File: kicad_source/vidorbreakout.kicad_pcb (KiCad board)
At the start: 2 copper layers, 40 x 46.5 mm, 12 parts, among them CN1 TE_2041119-2, CN2 CONN_01X18, CN3 CONN_01X18

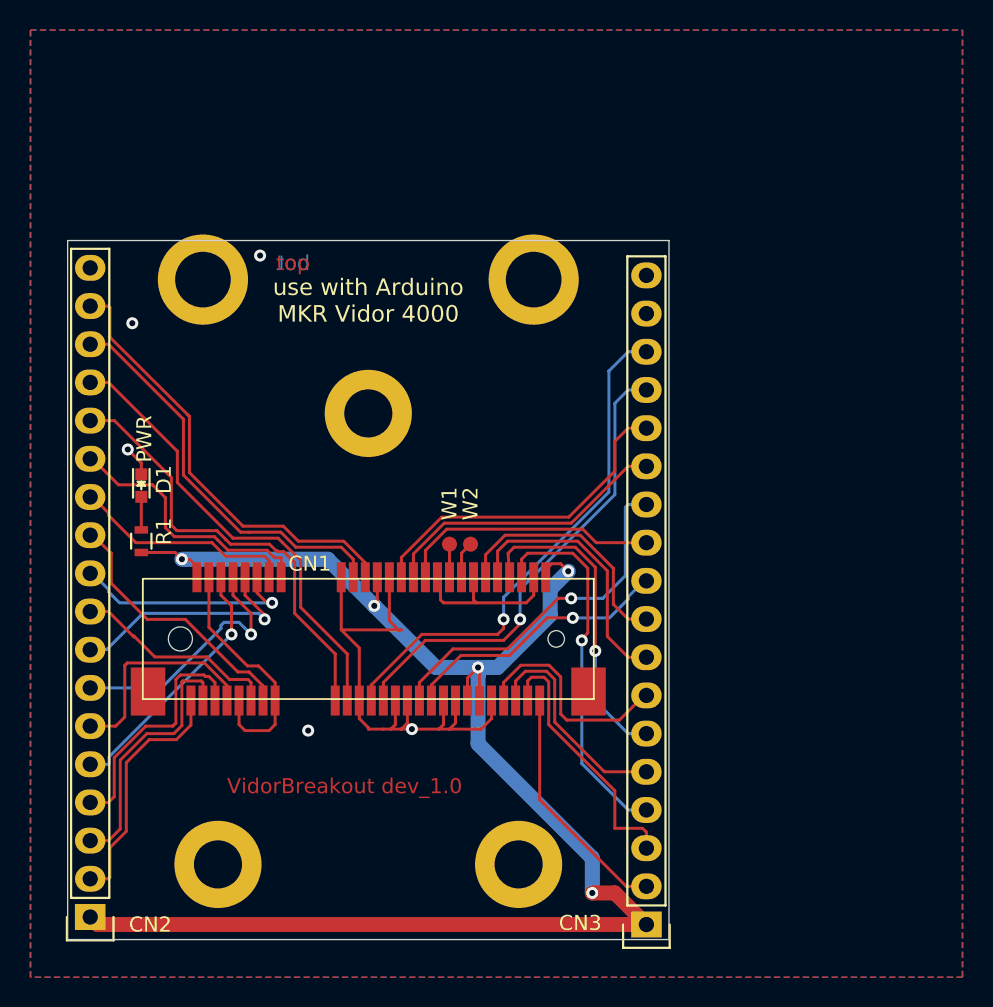
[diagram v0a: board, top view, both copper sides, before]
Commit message: aligned pin header to grid
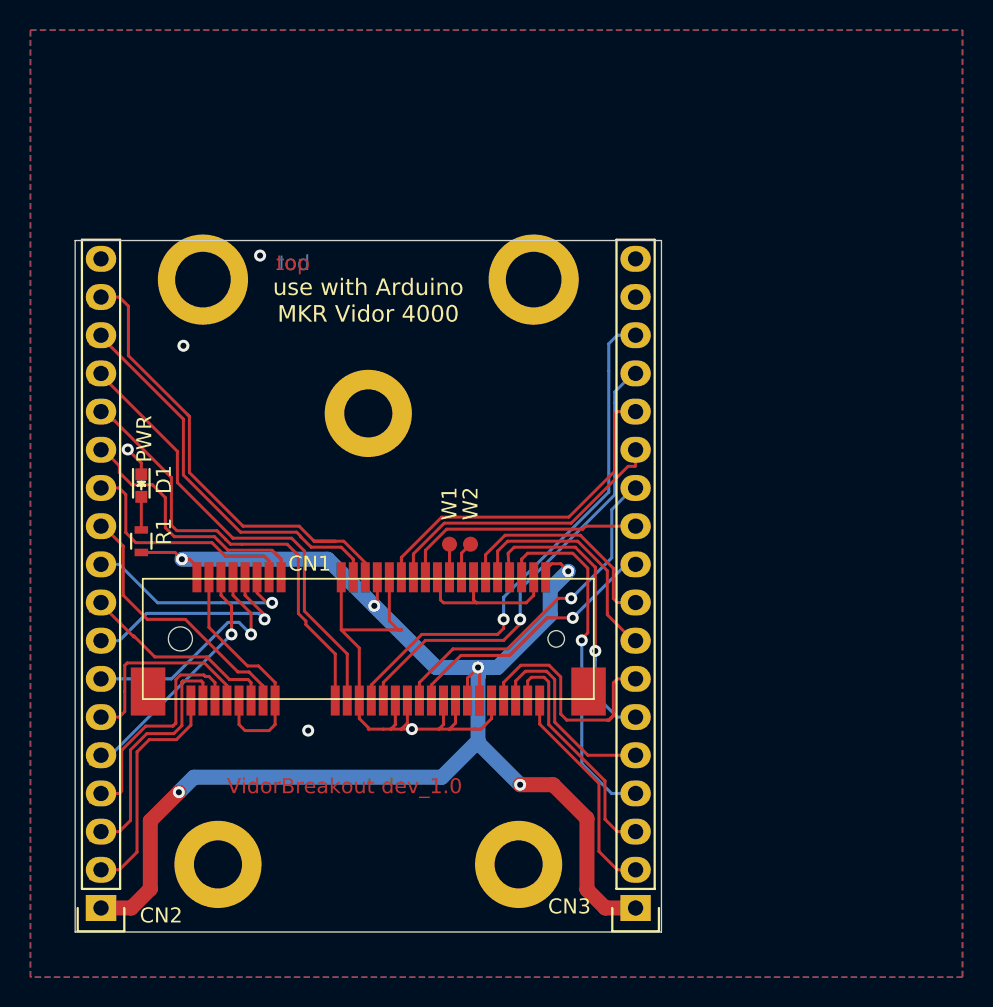
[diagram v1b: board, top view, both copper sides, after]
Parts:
- moved CN3 1.31 mm to (112.8, 147.9)
- moved CN2 0.94 mm to (77.2, 147.9)
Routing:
- net +3V3: track 106.0 -> 101.7 mm, vias 5 -> 6
- net /PEX_RST: track 29.7 -> 32.6 mm
- net /PEX_PIN44: track 17.7 -> 15.6 mm
- net /PEX_PIN49: track 17.8 -> 16.0 mm
- net /PEX_PIN45: track 14.8 -> 16.4 mm
- net /PEX_PIN51: track 16.1 -> 14.6 mm
- net /PEX_PIN46: track 21.3 -> 19.9 mm
- net /PEX_PIN42: track 16.5 -> 15.1 mm
- net /PEX_PIN7: track 14.5 -> 13.3 mm
- net /PEX_PIN47: track 14.7 -> 13.5 mm
- net /PEX_PIN48: track 24.9 -> 23.7 mm
- net /PEX_PIN8: track 17.3 -> 16.2 mm
- net /PEX_PIN31: track 23.9 -> 22.8 mm
- net /PEX_PIN32: track 17.4 -> 16.4 mm
- net /PEX_PIN14: track 14.8 -> 15.8 mm
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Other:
- board size 40 x 46.5 mm -> 39 x 46 mm

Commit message: reviewed  layout, added silkscreen, updated part values for aisler
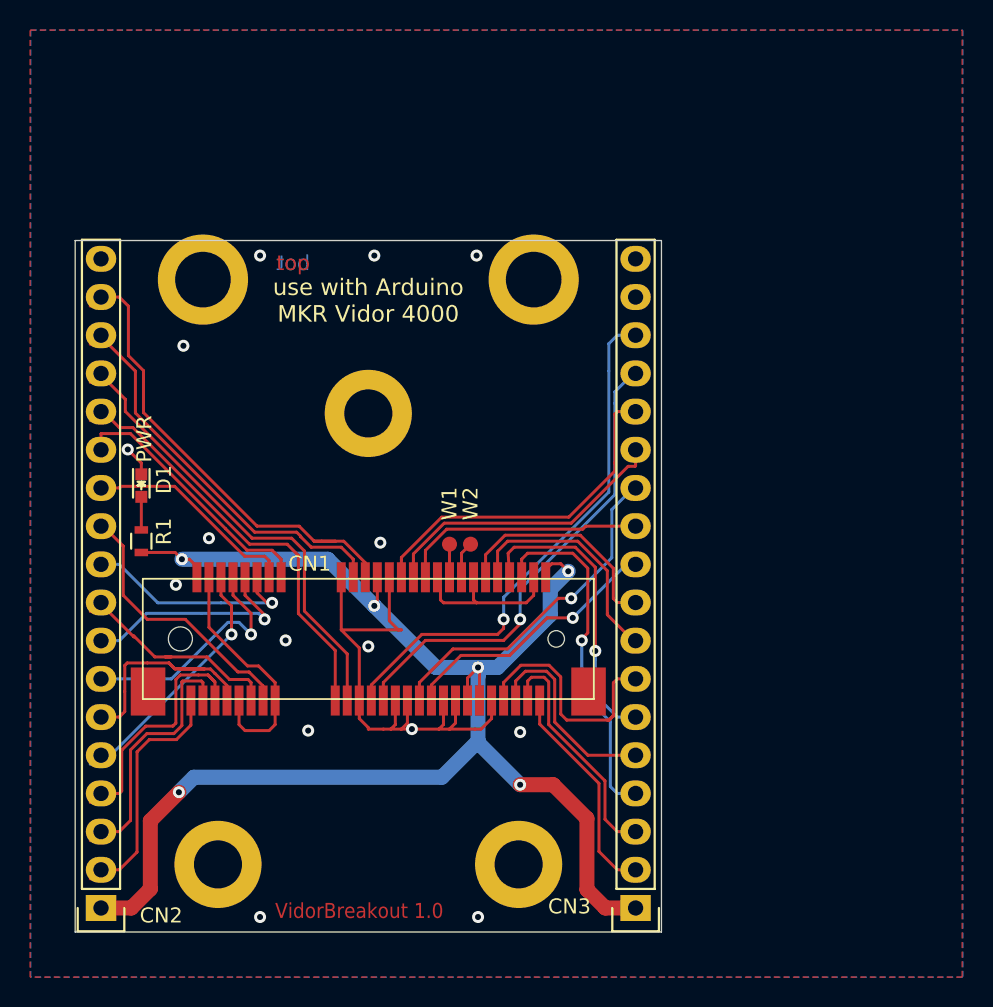
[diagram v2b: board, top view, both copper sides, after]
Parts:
- added G***: generationmake_logo, labels:generationmake_logo, B.Cu at (95.1, 126.2)
- added G***: generationmake_small_solder, labels:generationmake_small_solder, F.Cu at (94.9, 146.3)
- D1: value Led yellow -> 150060YS75000
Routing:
- net /PEX_PIN7: track 13.3 -> 15.8 mm
- net /PEX_PIN14: track 15.8 -> 14.4 mm
- net /WM_PIO24: track 30.1 -> 29.0 mm
- net /WM_PIO25: track 31.2 -> 30.5 mm
- net /PEX_PIN5: track 16.8 -> 17.4 mm
- net /PEX_RST: track 32.6 -> 32.0 mm
- net /PEX_PIN20: track 26.8 -> 26.3 mm
- net GND: vias 5 -> 15
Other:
- board text added: "3V3"
- board text added: "GND"
- board text added: "P1"
- board text added: "P10"
- board text added: "P11"
- board text added: "P12"
- board text added: "P13"
- board text added: "P14"
- board text added: "P16"
- board text added: "P20"
- board text added: "P23"
- board text added: "P25"
- board text added: "P28"
- board text added: "P3"
- board text added: "P30"
- board text added: "P31"
- board text added: "P32"
- board text added: "P33"
- board text added: "P42"
- board text added: "P44"
- board text added: "P45"
- board text added: "P46"
- board text added: "P47"
- board text added: "P48"
- board text added: "P49"
- board text added: "P5"
- board text added: "P51"
- board text added: "P6"
- board text added: "P7"
- board text added: "P8"
- board text added: "RST"
- board text added: "VidorBreakout 1.0"
- board text added: "WM_PIO24"
- board text added: "WM_PIO25"
- board text removed: "VidorBreakout dev_1.0"

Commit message: added pin description on bottom silk screen
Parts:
- moved G*** 7.43 mm to (97.7, 133.2), turned to 270 degrees
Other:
- board text added: "P10 (3)"
- board text added: "P11(19)"
- board text added: "P12(4)"
- board text added: "P13(20)"
- board text added: "P14(5)"
- board text added: "P16(6)"
- board text added: "P20(7)"
- board text added: "P23(21)"
- board text added: "P25(22)"
- board text added: "P28(8)"
- board text added: "P30(9)pu"
- board text added: "P31(23)"
- board text added: "P32(10)pu"
- board text added: "P33(24)"
- board text added: "P42(11)"
- board text added: "P44(12)"
- board text added: "P45(13)"
- board text added: "P46(14)"
- board text added: "P47(15)"
- board text added: "P48(16)"
- board text added: "P49 (17)"
- board text added: "P51 (18)"
- board text added: "P6(1)"
- board text added: "P8(2)"
- board text added: "RST (0)pu"
- board text removed: "P10"
- board text removed: "P11"
- board text removed: "P12"
- board text removed: "P13"
- board text removed: "P14"
- board text removed: "P16"
- board text removed: "P20"
- board text removed: "P23"
- board text removed: "P25"
- board text removed: "P28"
- board text removed: "P30"
- board text removed: "P31"
- board text removed: "P32"
- board text removed: "P33"
- board text removed: "P42"
- board text removed: "P44"
- board text removed: "P45"
- board text removed: "P46"
- board text removed: "P47"
- board text removed: "P48"
- board text removed: "P49"
- board text removed: "P51"
- board text removed: "P6"
- board text removed: "P8"
- board text removed: "RST"
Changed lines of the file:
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@@
   )
   (module labels:generationmake_logo (layer B.Cu)
-    (at 95.145 126.205 180)
-    (fp_text reference G*** (at 0 0) (layer B.SilkS) hide
+    (at 97.685 133.19 270)
+    (fp_text reference G*** (at 0 0 90) (layer B.SilkS) hide
       (effects (font (size 1.524 1.524) (thickness 0.3)) (justify mirror))
     )
-    (fp_text value generationmake_logo (at 0.75 0) (layer B.SilkS) hide
+    (fp_text value generationmake_logo (at 0.75 0 90) (layer B.SilkS) hide
       (effects (font (size 1.524 1.524) (thickness 0.3)) (justify mirror))
     )
@@
     (effects (font (size 1 1) (thickness 0.15)) (justify left mirror))
   )
-  (gr_text P51 (at 111.02 145.255) (layer B.SilkS)
-    (effects (font (size 1 1) (thickness 0.15)) (justify left mirror))
-  )
-  (gr_text P49 (at 111.02 142.715) (layer B.SilkS)
-    (effects (font (size 1 1) (thickness 0.15)) (justify left mirror))
-  )
-  (gr_text P48 (at 111.02 140.175) (layer B.SilkS)
-    (effects (font (size 1 1) (thickness 0.15)) (justify left mirror))
-  )
-  (gr_text P47 (at 111.02 137.635) (layer B.SilkS)
-    (effects (font (size 1 1) (thickness 0.15)) (justify left mirror))
-  )
-  (gr_text P46 (at 111.02 135.095) (layer B.SilkS)
-    (effects (font (size 1 1) (thickness 0.15)) (justify left mirror))
-  )
-  (gr_text P45 (at 111.02 132.555) (layer B.SilkS)
-    (effects (font (size 1 1) (thickness 0.15)) (justify left mirror))
-  )
-  (gr_text P44 (at 111.02 130.015) (layer B.SilkS)
-    (effects (font (size 1 1) (thickness 0.15)) (justify left mirror))
-  )
-  (gr_text P42 (at 111.02 127.475) (layer B.SilkS)
-    (effects (font (size 1 1) (thickness 0.15)) (justify left mirror))
-  )
-  (gr_text P33 (at 111.02 124.935) (layer B.SilkS)
-    (effects (font (size 1 1) (thickness 0.15)) (justify left mirror))
-  )
-  (gr_text P32 (at 111.02 122.395) (layer B.SilkS)
-    (effects (font (size 1 1) (thickness 0.15)) (justify left mirror))
-  )
-  (gr_text P31 (at 111.02 119.855) (layer B.SilkS)
-    (effects (font (size 1 1) (thickness 0.15)) (justify left mirror))
-  )
-  (gr_text P30 (at 111.02 117.315) (layer B.SilkS)
-    (effects (font (size 1 1) (thickness 0.15)) (justify left mirror))
-  )
-  (gr_text P28 (at 111.02 114.775) (layer B.SilkS)
-    (effects (font (size 1 1) (thickness 0.15)) (justify left mirror))
-  )
-  (gr_text P25 (at 111.02 112.235) (layer B.SilkS)
-    (effects (font (size 1 1) (thickness 0.15)) (justify left mirror))
-  )
-  (gr_text P23 (at 111.02 109.695) (layer B.SilkS)
+  (gr_text "P51        (18)" (at 111.02 145.255) (layer B.SilkS)
+    (effects (font (size 1 1) (thickness 0.15)) (justify left mirror))
+  )
+  (gr_text "P49        (17)" (at 111.02 142.715) (layer B.SilkS)
+    (effects (font (size 1 1) (thickness 0.15)) (justify left mirror))
+  )
+  (gr_text "P48(16)" (at 111.02 140.175) (layer B.SilkS)
+    (effects (font (size 1 1) (thickness 0.15)) (justify left mirror))
+  )
+  (gr_text "P47(15)" (at 111.02 137.635) (layer B.SilkS)
+    (effects (font (size 1 1) (thickness 0.15)) (justify left mirror))
+  )
+  (gr_text "P46(14)" (at 111.02 135.095) (layer B.SilkS)
+    (effects (font (size 1 1) (thickness 0.15)) (justify left mirror))
+  )
+  (gr_text "P45(13)" (at 111.02 132.555) (layer B.SilkS)
+    (effects (font (size 1 1) (thickness 0.15)) (justify left mirror))
+  )
+  (gr_text "P44(12)" (at 111.02 130.015) (layer B.SilkS)
+    (effects (font (size 1 1) (thickness 0.15)) (justify left mirror))
+  )
+  (gr_text "P42(11)" (at 111.02 127.475) (layer B.SilkS)
+    (effects (font (size 1 1) (thickness 0.15)) (justify left mirror))
+  )
+  (gr_text "P33(24)" (at 111.02 124.935) (layer B.SilkS)
+    (effects (font (size 1 1) (thickness 0.15)) (justify left mirror))
+  )
+  (gr_text "P32(10)pu" (at 111.02 122.395) (layer B.SilkS)
+    (effects (font (size 1 1) (thickness 0.15)) (justify left mirror))
+  )
+  (gr_text "P31(23)" (at 111.02 119.855) (layer B.SilkS)
+    (effects (font (size 1 1) (thickness 0.15)) (justify left mirror))
+  )
+  (gr_text "P30(9)pu" (at 111.02 117.315) (layer B.SilkS)
+    (effects (font (size 1 1) (thickness 0.15)) (justify left mirror))
+  )
+  (gr_text "P28(8)" (at 111.02 114.775) (layer B.SilkS)
+    (effects (font (size 1 1) (thickness 0.15)) (justify left mirror))
+  )
+  (gr_text "P25(22)" (at 111.02 112.235) (layer B.SilkS)
+    (effects (font (size 1 1) (thickness 0.15)) (justify left mirror))
+  )
+  (gr_text "P23(21)" (at 111.02 109.695) (layer B.SilkS)
     (effects (font (size 1 1) (thickness 0.15)) (justify left mirror))
   )
@@
     (effects (font (size 1 1) (thickness 0.15)) (justify right mirror))
   )
-  (gr_text RST (at 78.635 107.155) (layer B.SilkS)
-    (effects (font (size 1 1) (thickness 0.15)) (justify right mirror))
-  )
-  (gr_text P20 (at 78.635 109.695) (layer B.SilkS)
+  (gr_text "RST    (0)pu" (at 78.635 107.155) (layer B.SilkS)
+    (effects (font (size 1 1) (thickness 0.15)) (justify right mirror))
+  )
+  (gr_text "P20(7)" (at 78.635 109.695) (layer B.SilkS)
     (effects (font (size 1 1) (thickness 0.15)) (justify right mirror))
   )
@@
     (effects (font (size 1 1) (thickness 0.15)) (justify right mirror))
   )
-  (gr_text P16 (at 78.635 117.315) (layer B.SilkS)
-    (effects (font (size 1 1) (thickness 0.15)) (justify right mirror))
-  )
-  (gr_text P14 (at 78.635 119.855) (layer B.SilkS)
-    (effects (font (size 1 1) (thickness 0.15)) (justify right mirror))
-  )
-  (gr_text P13 (at 78.635 122.395) (layer B.SilkS)
-    (effects (font (size 1 1) (thickness 0.15)) (justify right mirror))
-  )
-  (gr_text P12 (at 78.635 124.935) (layer B.SilkS)
-    (effects (font (size 1 1) (thickness 0.15)) (justify right mirror))
-  )
-  (gr_text P11 (at 78.635 127.475) (layer B.SilkS)
-    (effects (font (size 1 1) (thickness 0.15)) (justify right mirror))
-  )
-  (gr_text P10 (at 78.635 130.015) (layer B.SilkS)
-    (effects (font (size 1 1) (thickness 0.15)) (justify right mirror))
-  )
-  (gr_text P8 (at 78.635 132.555) (layer B.SilkS)
+  (gr_text "P16(6)" (at 78.635 117.315) (layer B.SilkS)
+    (effects (font (size 1 1) (thickness 0.15)) (justify right mirror))
+  )
+  (gr_text "P14(5)" (at 78.635 119.855) (layer B.SilkS)
+    (effects (font (size 1 1) (thickness 0.15)) (justify right mirror))
+  )
+  (gr_text "P13(20)" (at 78.635 122.395) (layer B.SilkS)
+    (effects (font (size 1 1) (thickness 0.15)) (justify right mirror))
+  )
+  (gr_text "P12(4)" (at 78.635 124.935) (layer B.SilkS)
+    (effects (font (size 1 1) (thickness 0.15)) (justify right mirror))
+  )
+  (gr_text "P11(19)" (at 78.635 127.475) (layer B.SilkS)
+    (effects (font (size 1 1) (thickness 0.15)) (justify right mirror))
+  )
+  (gr_text "P10   (3)" (at 78.635 130.015) (layer B.SilkS)
+    (effects (font (size 1 1) (thickness 0.15)) (justify right mirror))
+  )
+  (gr_text "P8(2)" (at 78.635 132.555) (layer B.SilkS)
     (effects (font (size 1 1) (thickness 0.15)) (justify right mirror))
   )
@@
     (effects (font (size 1 1) (thickness 0.15)) (justify right mirror))
   )
-  (gr_text P6 (at 78.635 137.635) (layer B.SilkS)
-    (effects (font (size 1 1) (thickness 0.15)) (justify right mirror))
-  )
+  (gr_text "P6(1)" (at 78.635 137.635) (layer B.SilkS)
+    (effects (font (size 1 1) (thickness 0.15)) (justify right mirror))
+  )
